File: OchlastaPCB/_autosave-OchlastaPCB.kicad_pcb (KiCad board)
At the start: 4 copper layers, 175.1 x 89.9 mm, 37 parts, among them J1 XT60PW-M, J2 5V, U1 AP64501SP-13, U2 AP3429, U3 STM32F334R8Tx

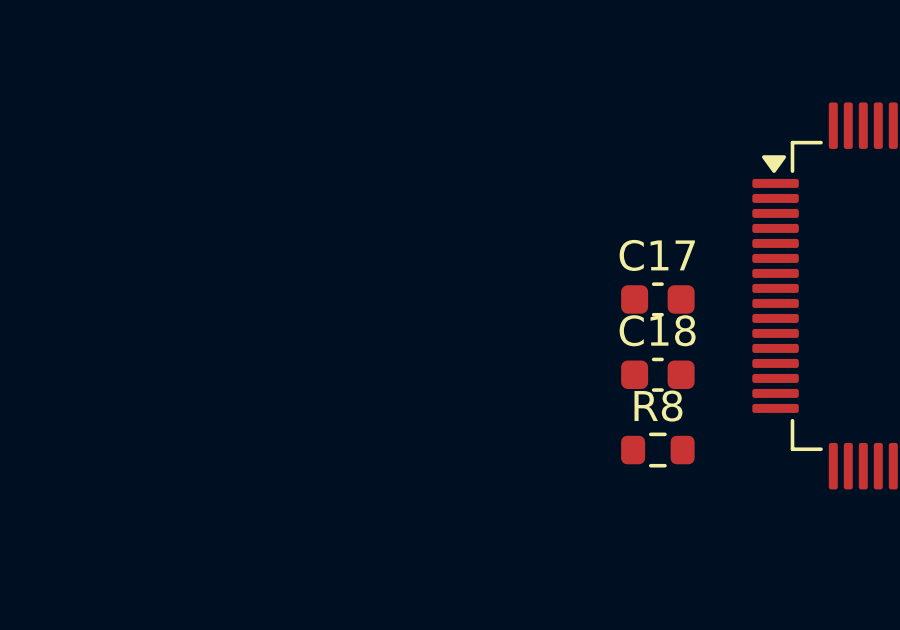
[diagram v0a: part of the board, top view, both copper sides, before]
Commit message: Power cascade for MCU schematics, created few components...
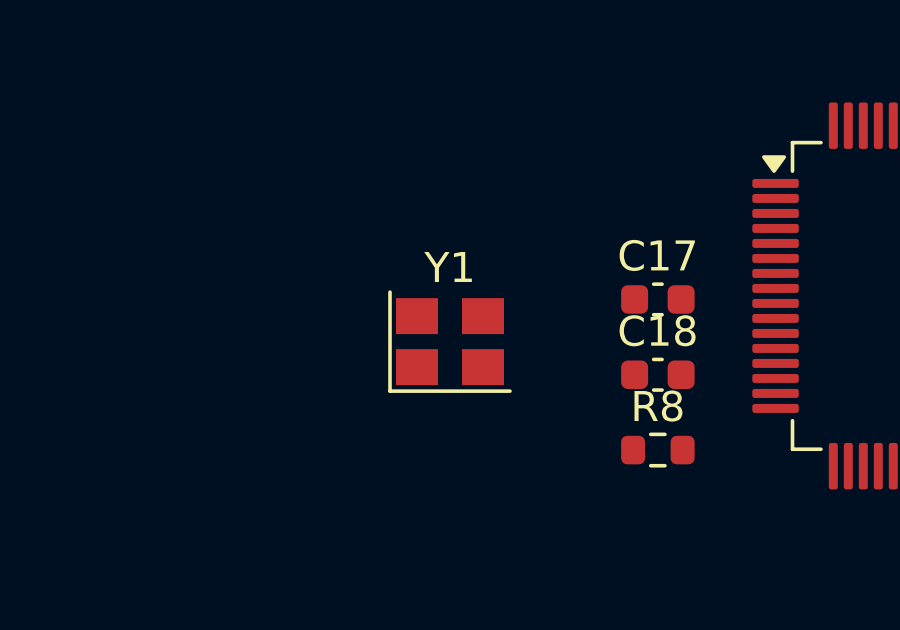
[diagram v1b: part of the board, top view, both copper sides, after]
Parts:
- added Y1: Crystal_GND24, Crystal:Crystal_SMD_3225-4Pin_3.2x2.5mm, F.Cu at (171.5, 94.0)
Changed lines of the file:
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@@
+		)
+	)
+	(footprint "Crystal:Crystal_SMD_3225-4Pin_3.2x2.5mm"
+		(layer "F.Cu")
+		(at 171.493 94.019)
+		(descr "SMD Crystal SERIES SMD3225/4 http://www.txccrystal.com/images/pdf/7m-accuracy.pdf, 3.2x2.5mm^2 package")
+		(tags "SMD SMT crystal")
+		(property "Reference" "Y1"
+			(at 0 -2.45 0)
+			(layer "F.SilkS")
+			(effects
+				(font
+					(size 1 1)
+					(thickness 0.15)
+				)
+			)
+		)
+		(property "Value" "Crystal_GND24"
+			(at 0 2.45 0)
+			(layer "F.Fab")
+			(effects
+				(font
+					(size 1 1)
+					(thickness 0.15)
+				)
+			)
+		)
+		(property "Datasheet" ""
+			(at 0 0 0)
+			(unlocked yes)
+			(layer "F.Fab")
+			(hide yes)
+			(effects
+				(font
+					(size 1.27 1.27)
+					(thickness 0.15)
+				)
+			)
+		)
+		(property "Description" "Four pin crystal, GND on pins 2 and 4"
+			(at 0 0 0)
+			(unlocked yes)
+			(layer "F.Fab")
+			(hide yes)
+			(effects
+				(font
+					(size 1.27 1.27)
+					(thickness 0.15)
+				)
+			)
+		)
+		(property ki_fp_filters "Crystal*")
+		(sheetname "/")
+		(sheetfile "OchlastaPCB.kicad_sch")
+		(attr smd)
+		(fp_line
+			(start -2 -1.65)
+			(end -2 1.65)
+			(stroke
+				(width 0.12)
+				(type solid)
+			)
+			(layer "F.SilkS")
+		)
+		(fp_line
+			(start -2 1.65)
+			(end 2 1.65)
+			(stroke
+				(width 0.12)
+				(type solid)
+			)
+			(layer "F.SilkS")
+		)
+		(fp_line
+			(start -2.1 -1.7)
+			(end -2.1 1.7)
+			(stroke
+				(width 0.05)
+				(type solid)
+			)
+			(layer "F.CrtYd")
+		)
+		(fp_line
+			(start -2.1 1.7)
+			(end 2.1 1.7)
+			(stroke
+				(width 0.05)
+				(type solid)
+			)
+			(layer "F.CrtYd")
+		)
+		(fp_line
+			(start 2.1 -1.7)
+			(end -2.1 -1.7)
+			(stroke
+				(width 0.05)
+				(type solid)
+			)
+			(layer "F.CrtYd")
+		)
+		(fp_line
+			(start 2.1 1.7)
+			(end 2.1 -1.7)
+			(stroke
+				(width 0.05)
+				(type solid)
+			)
+			(layer "F.CrtYd")
+		)
+		(fp_line
+			(start -1.6 -1.25)
+			(end -1.6 1.25)
+			(stroke
+				(width 0.1)
+				(type solid)
+			)
+			(layer "F.Fab")
+		)
+		(fp_line
+			(start -1.6 0.25)
+			(end -0.6 1.25)
+			(stroke
+				(width 0.1)
+				(type solid)
+			)
+			(layer "F.Fab")
+		)
+		(fp_line
+			(start -1.6 1.25)
+			(end 1.6 1.25)
+			(stroke
+				(width 0.1)
+				(type solid)
+			)
+			(layer "F.Fab")
+		)
+		(fp_line
+			(start 1.6 -1.25)
+			(end -1.6 -1.25)
+			(stroke
+				(width 0.1)
+				(type solid)
+			)
+			(layer "F.Fab")
+		)
+		(fp_line
+			(start 1.6 1.25)
+			(end 1.6 -1.25)
+			(stroke
+				(width 0.1)
+				(type solid)
+			)
+			(layer "F.Fab")
+		)
+		(fp_text user "${REFERENCE}"
+			(at 0 0 0)
+			(layer "F.Fab")
+			(effects
+				(font
+					(size 0.7 0.7)
+					(thickness 0.105)
+				)
+			)
+		)
+		(pad "1" smd rect
+			(at -1.1 0.85)
+			(size 1.4 1.2)
+			(layers "F.Cu" "F.Mask" "F.Paste")
+			(net 78 "Net-(C17-Pad1)")
+			(pinfunction "1")
+			(pintype "passive")
+		)
+		(pad "2" smd rect
+			(at 1.1 0.85)
+			(size 1.4 1.2)
+			(layers "F.Cu" "F.Mask" "F.Paste")
+			(net 2 "GND")
+			(pinfunction "2")
+			(pintype "passive")
+		)
+		(pad "3" smd rect
+			(at 1.1 -0.85)
+			(size 1.4 1.2)
+			(layers "F.Cu" "F.Mask" "F.Paste")
+			(net 79 "Net-(C18-Pad1)")
+			(pinfunction "3")
+			(pintype "passive")
+		)
+		(pad "4" smd rect
+			(at -1.1 -0.85)
+			(size 1.4 1.2)
+			(layers "F.Cu" "F.Mask" "F.Paste")
+			(net 2 "GND")
+			(pinfunction "4")
+			(pintype "passive")
+		)
+		(embedded_fonts no)
+		(model "${KICAD9_3DMODEL_DIR}/Crystal.3dshapes/Crystal_SMD_3225-4Pin_3.2x2.5mm.wrl"
+			(offset
+				(xyz 0 0 0)
+			)
+			(scale
+				(xyz 1 1 1)
+			)
+			(rotate
+				(xyz 0 0 0)
+			)
 		)
 	)
